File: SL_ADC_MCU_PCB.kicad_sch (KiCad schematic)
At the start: 0 parts

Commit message: Added ADS8528 footprint
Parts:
- added IC1: ADS8528SPM, QFP50P1200X1200X160-64N, symbol ADS8528:ADS8528SPM

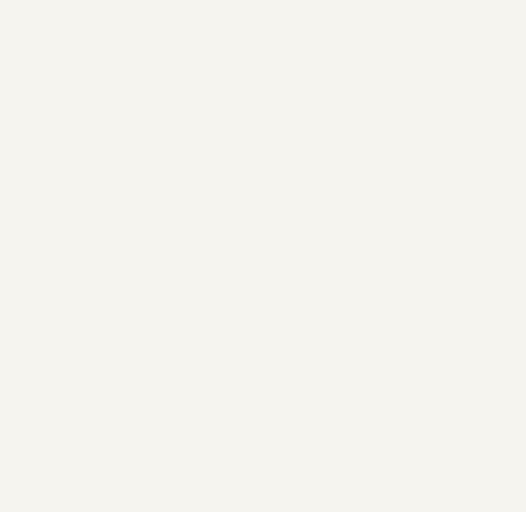
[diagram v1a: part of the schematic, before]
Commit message: made custom model for STM32H7 sus amazon board, currently does not work but will fix
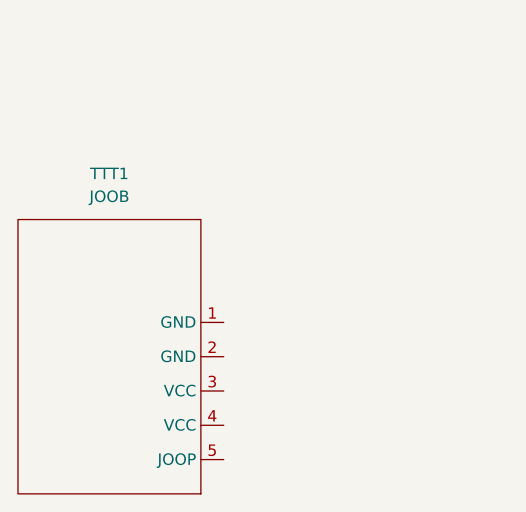
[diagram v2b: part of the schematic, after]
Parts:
- added TTT1: JOOB, TESTY:TESTY, symbol TESTY:TESTY
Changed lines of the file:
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@@
+		)
+	)
+	(symbol
+		(lib_id "TESTY:TESTY")
+		(at 77.47 125.73 0)
+		(unit 1)
+		(exclude_from_sim no)
+		(in_bom yes)
+		(on_board yes)
+		(dnp no)
+		(fields_autoplaced yes)
+		(property "Reference" "TTT1"
+			(at 64.77 107.95 0)
+			(effects
+				(font
+					(size 1.27 1.27)
+				)
+			)
+		)
+		(property "Value" "JOOB"
+			(at 64.77 110.49 0)
+			(effects
+				(font
+					(size 1.27 1.27)
+				)
+			)
+		)
+		(property "Footprint" "TESTY:TESTY"
+			(at 77.47 125.73 0)
+			(effects
+				(font
+					(size 1.27 1.27)
+				)
+				(hide yes)
+			)
+		)
+		(property "Datasheet" ""
+			(at 77.47 125.73 0)
+			(effects
+				(font
+					(size 1.27 1.27)
+				)
+				(hide yes)
+			)
+		)
+		(property "Description" ""
+			(at 77.47 125.73 0)
+			(effects
+				(font
+					(size 1.27 1.27)
+				)
+				(hide yes)
+			)
+		)
+		(pin "2"
+		)
+		(pin "5"
+		)
+		(pin "1"
+		)
+		(pin "3"
+		)
+		(pin "4"
+		)
+		(instances
+			(project ""
+				(path "/3f4eb23c-7a54-403d-a4d1-8d06ed1540f4"
+					(reference "TTT1")
+					(unit 1)
+				)
+			)
 		)
 	)

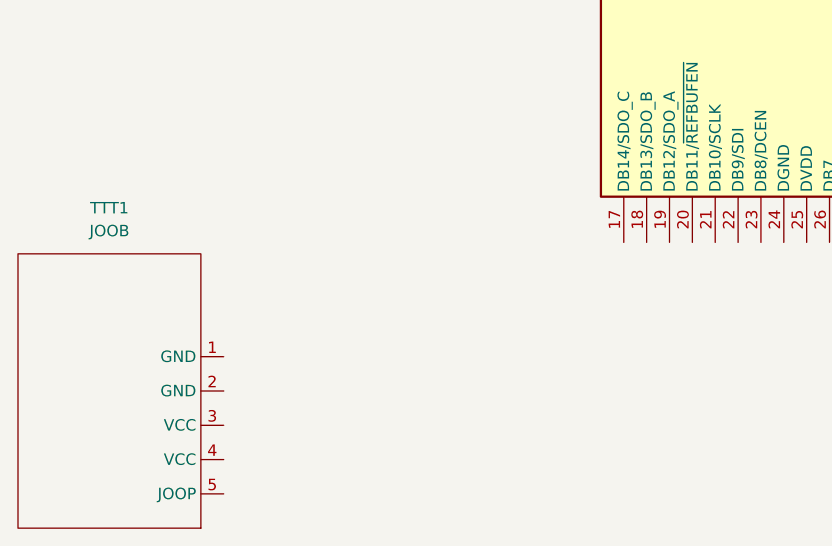
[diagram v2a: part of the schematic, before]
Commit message: added altium based schematic and footprint for the STM32 H7 dev board into additional docs
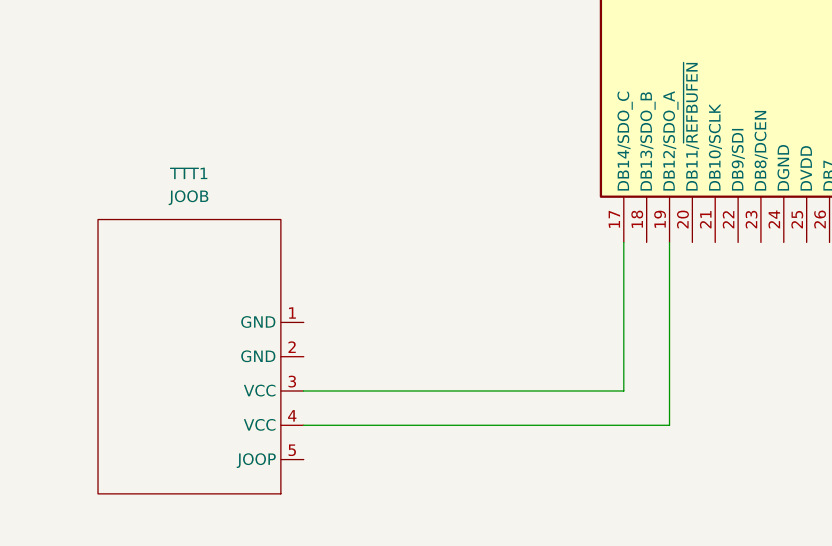
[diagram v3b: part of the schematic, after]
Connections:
- net at IC1.17 (DB14/SDO_C): now also TTT1.3 (VCC)
- net at IC1.19 (DB12/SDO_A): now also TTT1.4 (VCC)
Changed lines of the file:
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@@
 	(generator_version "9.0")
 	(paper "A4")
+	(wire
+		(pts
+			(xy 127 111.76) (xy 127 132.08)
+		)
+		(stroke
+			(width 0)
+			(type default)
+		)
+	)
+	(wire
+		(pts
+			(xy 86.36 128.27) (xy 121.92 128.27)
+		)
+		(stroke
+			(width 0)
+			(type default)
+		)
+	)
+	(wire
+		(pts
+			(xy 86.36 132.08) (xy 127 132.08)
+		)
+		(stroke
+			(width 0)
+			(type default)
+		)
+	)
+	(wire
+		(pts
+			(xy 121.92 128.27) (xy 121.92 111.76)
+		)
+		(stroke
+			(width 0)
+			(type default)
+		)
+	)
 	(symbol
 		(lib_id "ADS8528:ADS8528SPM")
@@
 	(symbol
 		(lib_id "TESTY:TESTY")
-		(at 77.47 125.73 0)
+		(at 86.36 121.92 0)
 		(unit 1)
 		(exclude_from_sim no)
@@
 		(fields_autoplaced yes)
 		(property "Reference" "TTT1"
-			(at 64.77 107.95 0)
+			(at 73.66 104.14 0)
 			(effects
 				(font
@@
 		)
 		(property "Value" "JOOB"
-			(at 64.77 110.49 0)
+			(at 73.66 106.68 0)
 			(effects
 				(font
@@
 		)
 		(property "Footprint" "TESTY:TESTY"
-			(at 77.47 125.73 0)
+			(at 86.36 121.92 0)
 			(effects
 				(font
@@
 		)
 		(property "Datasheet" ""
-			(at 77.47 125.73 0)
+			(at 86.36 121.92 0)
 			(effects
 				(font
@@
 		)
 		(property "Description" ""
-			(at 77.47 125.73 0)
-			(effects
-				(font
-					(size 1.27 1.27)
-				)
-				(hide yes)
-			)
+			(at 86.36 121.92 0)
+			(effects
+				(font
+					(size 1.27 1.27)
+				)
+				(hide yes)
+			)
+		)
+		(pin "5"
 		)
 		(pin "2"
 		)
-		(pin "5"
+		(pin "4"
 		)
 		(pin "1"
@@
 		(pin "3"
 		)
-		(pin "4"
-		)
 		(instances

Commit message: pushing again in case I didnt save things
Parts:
- removed TTT1: JOOB, TESTY:TESTY, symbol TESTY:TESTY
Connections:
- net -5V-HVSS: now reaches IC1.1 (HVSS)
- net RESET: now reaches IC1.10 (RESET)
- net REFEN/~WR: now reaches IC1.11 (REFEN/~{WR})
- net ~RD: now reaches IC1.12 (~{RD})
- net ~CS/~FS: now reaches IC1.13 (~{CS}/~{FS})
- net AVDD: now reaches IC1.14 (AVDD_2)
- net AVDD: now also IC1.4 (AVDD_1), IC1.45 (AVDD_3), IC1.52 (AVDD_4), IC1.57 (AVDD_5), IC1.61 (AVDD_6)
- net AGND: now reaches IC1.15 (AGND_2)
- net AGND: now also IC1.44 (AGND_3), IC1.5 (AGND_1), IC1.51 (AGND_4), IC1.58 (AGND_5), IC1.62 (AGND_6)
- net DB15: now reaches IC1.16 (DB15/SDO_D)
- net DB14: now reaches IC1.17 (DB14/SDO_C)
- net DB13: now reaches IC1.18 (DB13/SDO_B)
- net DB12: now reaches IC1.19 (DB12/SDO_A)
- net CH_D1: now reaches IC1.2 (CH_D1)
- net DB11: now reaches IC1.20 (DB11/~{REFBUFEN})
- net DB10: now reaches IC1.21 (DB10/SCLK)
- net DB9: now reaches IC1.22 (DB9/SDI)
- net DB8: now reaches IC1.23 (DB8/DCEN)
- net DGND: now reaches IC1.24 (DGND)
- net DVDD: now reaches IC1.25 (DVDD)
- net DB7: now reaches IC1.26 (DB7)
- net DB6: now reaches IC1.27 (DB6/SEL_B)
- net DB5: now reaches IC1.28 (DB5/SEL_CD)
- net DB4: now reaches IC1.29 (DB4)
- net REFDN: now reaches IC1.3 (REFDN)
- net DB3: now reaches IC1.30 (DB3/DCIN_A)
- net DB2: now reaches IC1.31 (DB2/DCIN_B)
- net DB1: now reaches IC1.32 (DB1/DCIN_C)
- net DB0: now reaches IC1.33 (DB0/DCIN_D)
- net RANGE/XCLK: now reaches IC1.34 (RANGE/XCLK)
- net BUSY/INT: now reaches IC1.35 (BUSY/INT)
- net ASLEEP: now reaches IC1.36 (ASLEEP)
- net CONVST_A: now reaches IC1.37 (CONVST_A)
- net CONVST_B: now reaches IC1.38 (CONVST_B)
- net CONVST_C: now reaches IC1.39 (CONVST_C)
- net CONVST_D: now reaches IC1.40 (CONVST_D)
- net ~HW/SW: now reaches IC1.41 (~{HW}/SW)
- net CH_A0: now reaches IC1.42 (CH_A0)
- net REFAP: now reaches IC1.43 (REFAP)
- net REFAN: now reaches IC1.46 (REFAN)
- net CH_A1: now reaches IC1.47 (CH_A1)
- net 5V-HVDD: now reaches IC1.48 (HVDD)
- net CH_B0: now reaches IC1.49 (CH_B0)
- net REFBP: now reaches IC1.50 (REFBP)
- net REFBN: now reaches IC1.53 (REFBN)
- net CH_B1: now reaches IC1.54 (CH_B1)
- net REFN: now reaches IC1.55 (REFN)
- net REFIO: now reaches IC1.56 (REFIO)
- net CH_C1: now reaches IC1.59 (CH_C1)
- net CH_C1: now also IC1.63 (REFCP)
- net REFDP: now reaches IC1.6 (REFDP)
- net REFCN: now reaches IC1.60 (REFCN)
- net CH_C0: now reaches IC1.64 (CH_C0)
- net CH_D0: now reaches IC1.7 (CH_D0)
- net ~PAR/SER: now reaches IC1.8 (~{PAR}/SER)
- net ~STBY: now reaches IC1.9 (~{STBY})

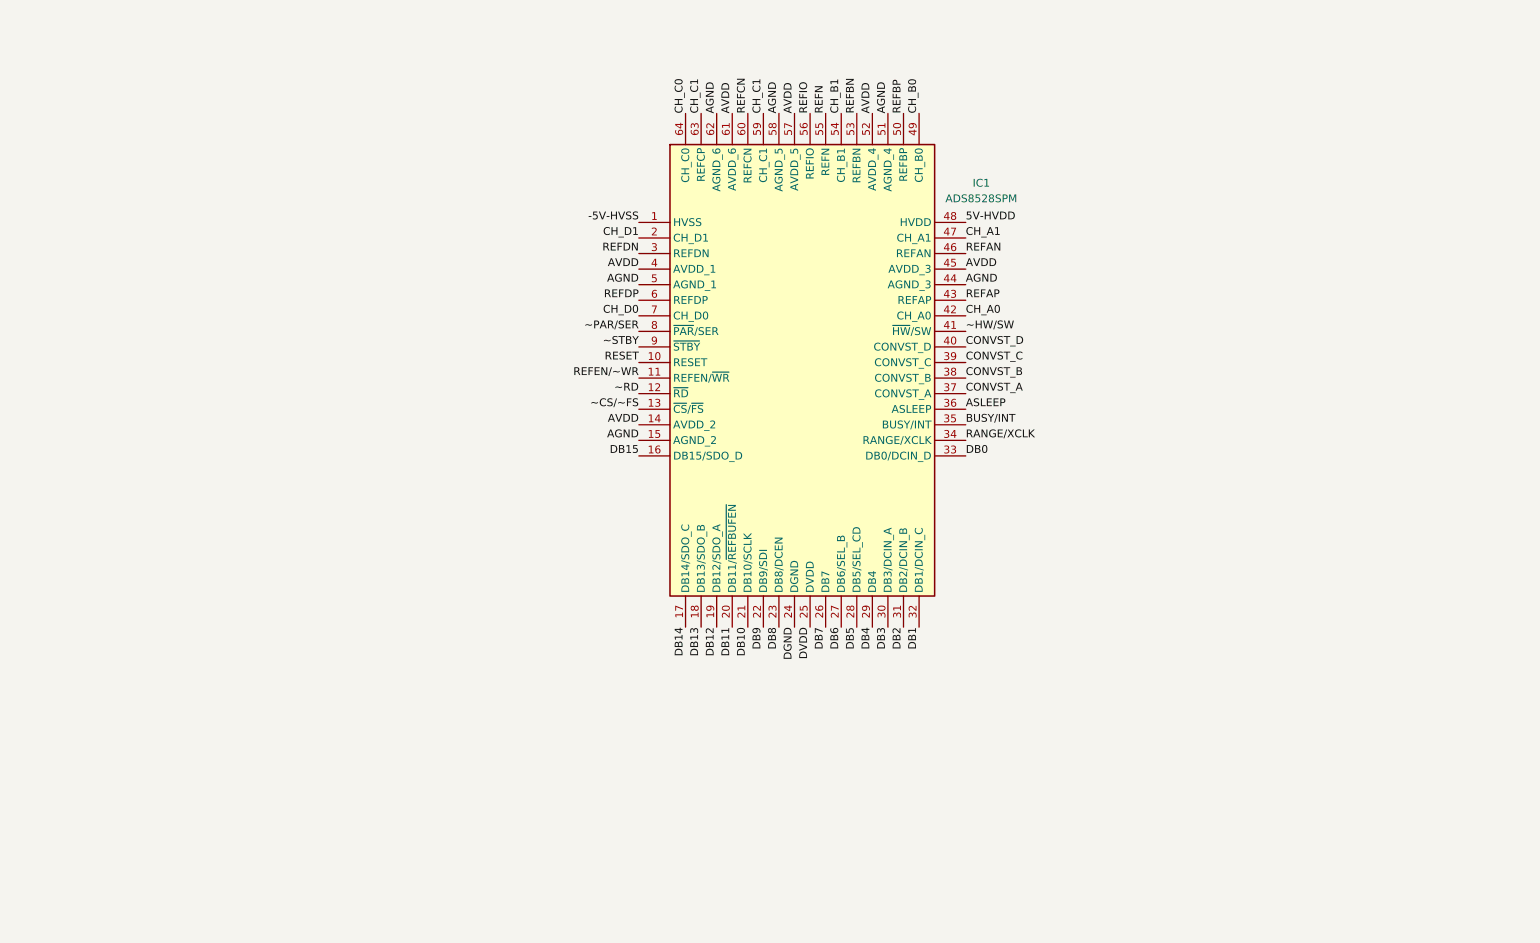
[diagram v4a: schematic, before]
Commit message: added decoupling capacitors for the AVDD to AGND for the ADC
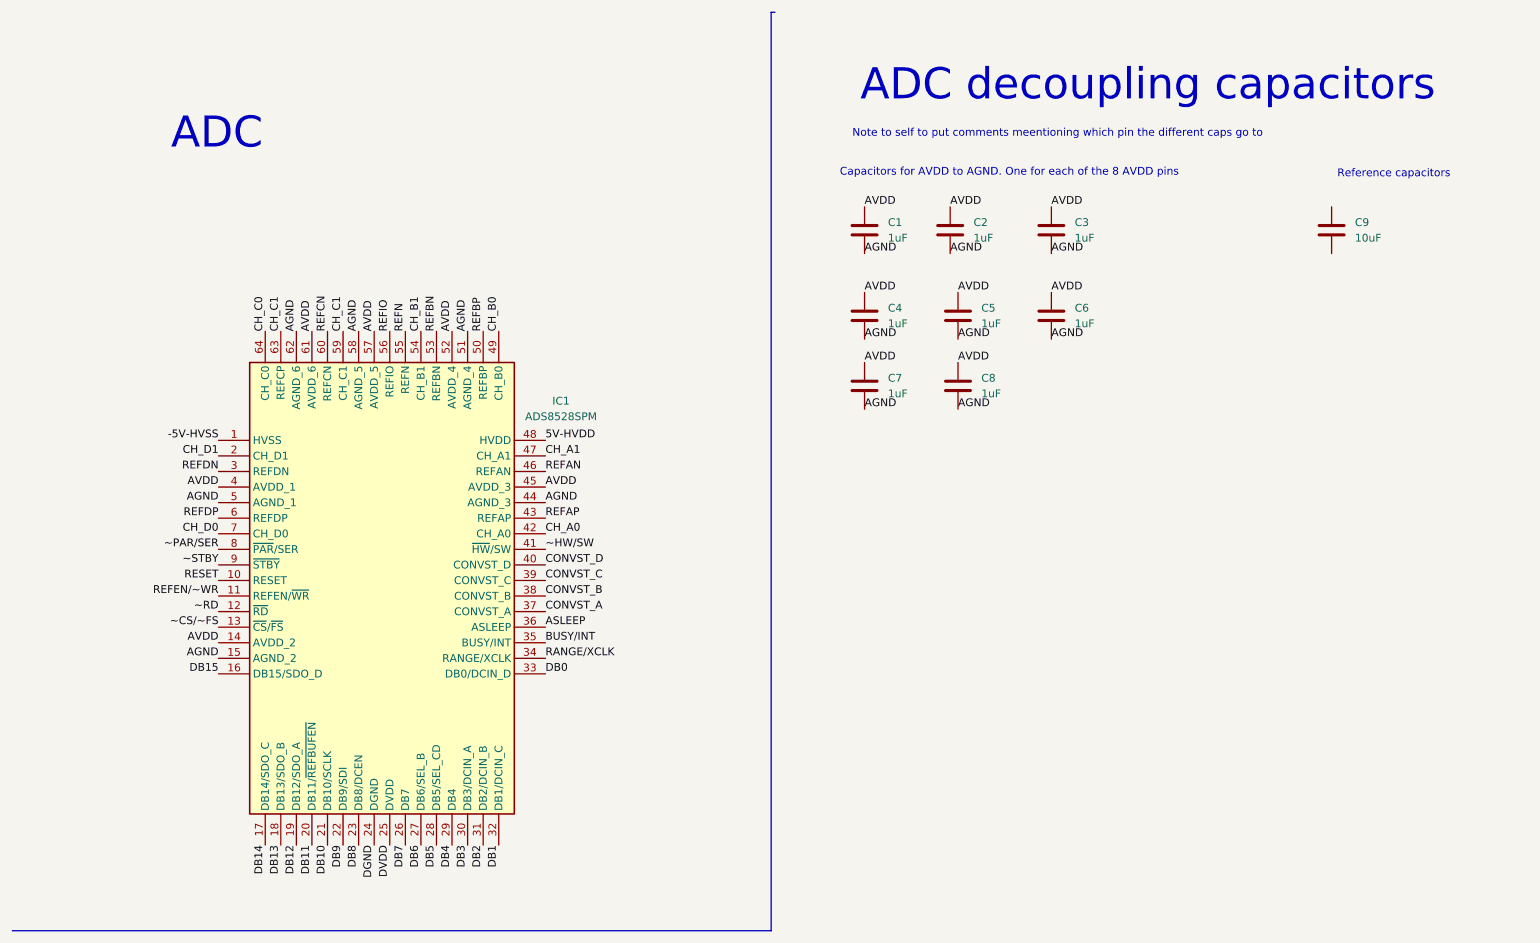
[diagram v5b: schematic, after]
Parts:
- added C1, C2, C3, C4, C5, C6, C7, C8: 1uF, Capacitor_SMD:C_0805_2012Metric_Pad1.18x1.45mm_HandSolder, symbol Device:C
- added C9: 10uF, Capacitor_SMD:C_0805_2012Metric_Pad1.18x1.45mm_HandSolder, symbol Device:C
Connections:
- net AGND: now also C1.2, C2.2, C3.2, C4.2, C5.2, C6.2, C7.2, C8.2
- net AVDD: now also C1.1, C2.1, C3.1, C4.1, C5.1, C6.1, C7.1, C8.1
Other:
- note added: "ADC"
- note added: "ADC decoupling capacitors"
- note added: "Capacitors for AVDD to AGND. One for each of the 8 AVDD pins"
- note added: "Note to self to put comments meentioning which pin the different caps go to"
- note added: "Reference capacitors"
- moved on the sheet: IC1

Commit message: Decided on connection convention between STM board and ADC, ensuring DB0 to DB11 are all on GPIO bank A for simultanious acquistion and CONVST A,B,C,and D are all on the same bank to be set simultaniously
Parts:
- added C10, C11, C12, C14, C16: 10uF, Capacitor_SMD:C_0805_2012Metric_Pad1.18x1.45mm_HandSolder, symbol Device:C
- added C13: 470nF, Capacitor_SMD:C_0805_2012Metric_Pad1.18x1.45mm_HandSolder, symbol Device:C
- added C15, C17, C18: 0.1uF, Capacitor_SMD:C_0805_2012Metric_Pad1.18x1.45mm_HandSolder, symbol Device:C
- added STM1: ~, STM32H7_knockoff:STM32H7_knockoff, symbol STM32H7_knockoff:STM32H7_knockoff
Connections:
- net REFAN is gone; now on net AGND: IC1.46 (REFAN)
- net REFBN is gone; now on net AGND: IC1.53 (REFBN)
- net REFCN is gone; now on net AGND: IC1.60 (REFCN)
- net REFDN is gone; now on net AGND: IC1.3 (REFDN)
- net -5V-HVSS: now also C16.1, C17.1
- net 5V-HVDD: now also C14.1, C15.1
- net AGND: now also C9.2, C10.2, C11.2, C12.2, C14.2, C15.2, C16.2, C17.2
- net ASLEEP: now also STM1.E2
- net BUSY/INT: now also STM1.B6
- net CONVST_A: now also STM1.D13
- net CONVST_B: now also STM1.D11
- net CONVST_C: now also STM1.D12
- net CONVST_D: now also STM1.D2
- net DB0: now also STM1.A0
- net DB1: now also STM1.A1
- net DB10: now also STM1.A11
- net DB11: now also STM1.A12
- net DB12: now also STM1.B8
- net DB13: now also STM1.B4
- net DB14: now also STM1.B5
- net DB15: now also STM1.B3
- net DB2: now also STM1.A2
- net DB3: now also STM1.A3
- net DB4: now also STM1.A4
- net DB5: now also STM1.A5
- net DB6: now also STM1.A6
- net DB7: now also STM1.A7
- net DB8: now also STM1.A9
- net DB9: now also STM1.A10
- net DGND: now also C18.2
- net DVDD: now also C18.1
- net RANGE/XCLK: now also STM1.B2
- net REFAP: now also C9.1
- net REFBP: now also C10.1
- net REFDP: now also C12.1
- net REFEN/~WR: now also STM1.E12
- net REFIO: now also C13.1
- net REFN: now also C13.2
- net RESET: now also STM1.E11
- net ~CS/~FS: now also STM1.E7
- net ~HW/SW: now also STM1.C12
- net ~PAR/SER: now also STM1.B10
- net ~RD: now also STM1.E10
- net ~STBY: now also STM1.E14
- new net REFCP: C11.1
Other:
- note added: "Decoupling caps for HVDD and HVSS"
- note added: "Digital decoupling cap"
- note added: "Double check if you can simply put the refAN refBN pins etc to ground I think thats how it works but double check"
- note added: "we have chosen to conenct the firsts 12 DB pins to the GPIO bank A The remaning 4 only provide a sign extension during the bulk of communication but will be needed for checking config regsiters"
- moved on the sheet: C1, C2, C3, C4, C5, C6, C7, C8, C9, IC1
